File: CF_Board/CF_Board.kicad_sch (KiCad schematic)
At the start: 24 parts, among them J1 Conn_02x04_Odd_Even, SW1 SW_DIP_x08, U1 74FCT16245, U2 74HCT245, U3 22V10, U4 74HCT688, U5 74HCT138, U6 22V10, U7 74LVC1G07, X1 DIN41612_03x32_ABC_VMEbus

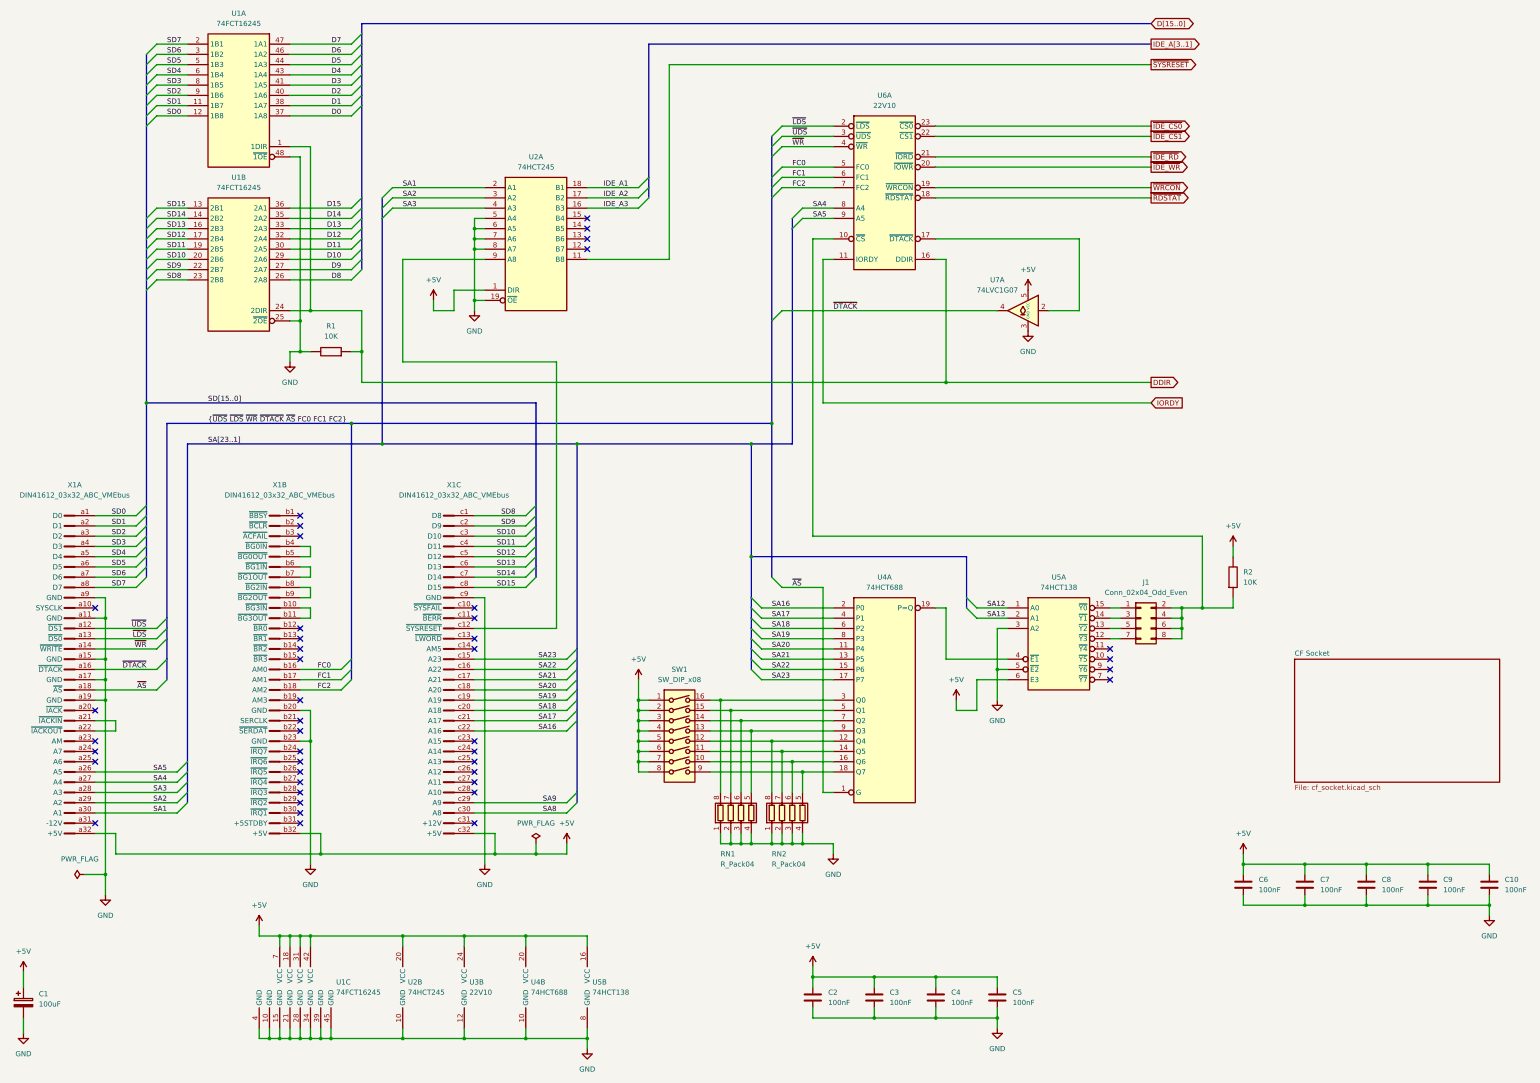
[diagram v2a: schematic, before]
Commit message: Starting PCB layout
* Rearranged signals in the schematic for easier routing
* Rough placement of components on PCB

Still needs a footprint for the CF socket
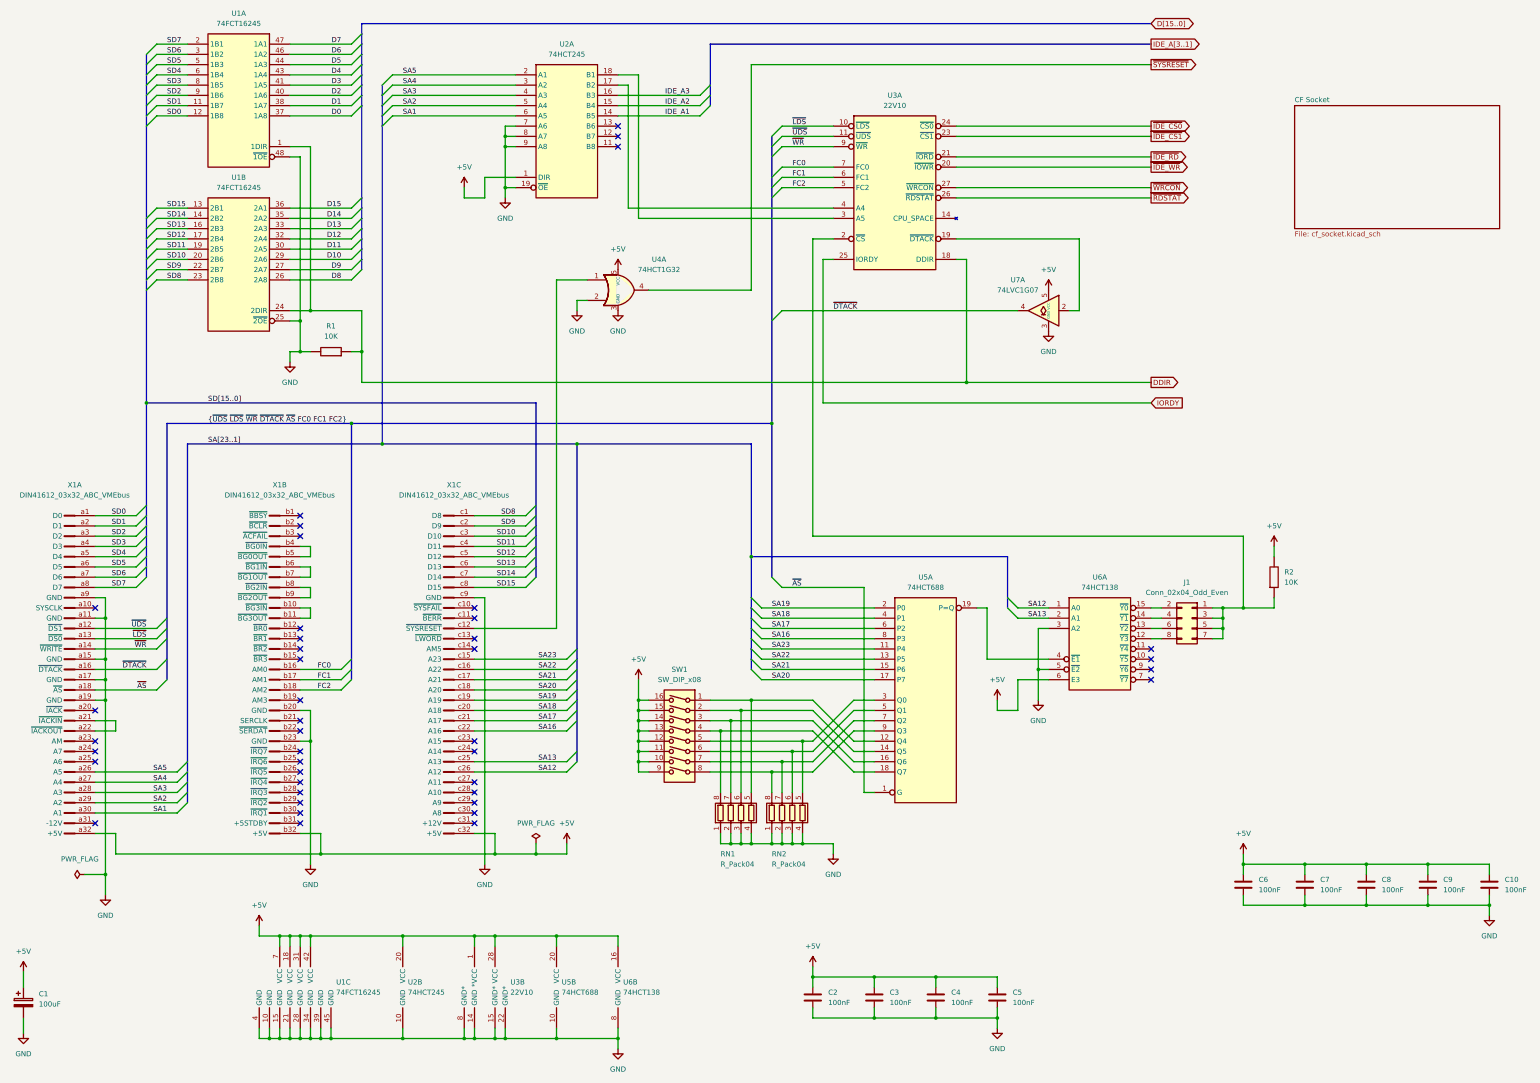
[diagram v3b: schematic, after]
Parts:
- added U4: 74HCT1G32, COMET_footprints:Package_SOT23-5, symbol COMET_symbols:74x1G32
- U3: renamed from U6; footprint Package_DIP:DIP-24_W7.62mm_Socket -> COMET_footprints:Package_PLCC-28_SMD_socket; symbol CF_Board:22V10 -> CF_Board:GAL
- U3: footprint Package_DIP:DIP-24_W7.62mm_Socket -> COMET_footprints:Package_PLCC-28_SMD_socket
- renumbered U4 to U5, U5 to U6
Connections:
- net +5V: now also SW1.10, SW1.11, SW1.12, SW1.13, SW1.14, SW1.15, SW1.16, SW1.9, U3.1 (*VCC), U3.28 (VCC), U4.5 (VCC); no longer SW1.1, SW1.2, SW1.3, SW1.4, SW1.5, SW1.6, SW1.7, SW1.8, U3.24 (VCC)
- net DDIR: now also U3.18 (DDIR); no longer U3.16 (DDIR)
- net FC0: now also U3.7 (FC0); no longer U3.5 (FC0)
- net FC2: now also U3.5 (FC2); no longer U3.7 (FC2)
- net GND: now also U2.9 (A8), U3.14 (GND), U3.15 (GND*), U3.22 (GND*), U3.8 (GND*), U4.2, U4.3 (GND); no longer U2.5 (A4), U2.6 (A5), U3.12 (GND)
- net IDE_A1: now also U2.14 (B5); no longer U2.18 (B1)
- net IDE_A2: now also U2.15 (B4); no longer U2.17 (B2)
- net IORDY: now also U3.25 (IORDY); no longer U3.11 (IORDY)
- net SA1: now also U2.6 (A5); no longer U2.2 (A1)
- net SA12: now also X1.c26 (A12)
- net SA13: now also X1.c25 (A13)
- net SA16: now also U5.8 (P3); no longer U5.2 (P0)
- net SA17: now also U5.6 (P2); no longer U5.4 (P1)
- net SA18: now also U5.4 (P1); no longer U5.6 (P2)
- net SA19: now also U5.2 (P0); no longer U5.8 (P3)
- net SA2: now also U2.5 (A4); no longer U2.3 (A2)
- net SA20: now also U5.17 (P7); no longer U5.11 (P4)
- net SA21: now also U5.15 (P6); no longer U5.13 (P5)
- net SA22: now also U5.13 (P5); no longer U5.15 (P6)
- net SA23: now also U5.11 (P4); no longer U5.17 (P7)
- net SA4: now also U2.3 (A2); no longer U3.8 (A4)
- net SA5: now also U2.2 (A1); no longer U3.9 (A5)
- net ~{IDE_CS0}: now also U3.24 (~{CS0}); no longer U3.23 (~{CS0})
- net ~{IDE_CS1}: now also U3.23 (~{CS1}); no longer U3.22 (~{CS1})
- net ~{LDS}: now also U3.10 (~{LDS}); no longer U3.2 (~{LDS})
- net ~{RDSTAT}: now also U3.26 (~{RDSTAT}); no longer U3.18 (~{RDSTAT})
- net ~{SYSRESET}: now also U4.4; no longer U2.11 (B8)
- net ~{UDS}: now also U3.11 (~{UDS}); no longer U3.3 (~{UDS})
- net ~{WRCON}: now also U3.27 (~{WRCON}); no longer U3.19 (~{WRCON})
- net ~{WR}: now also U3.9 (~{WR}); no longer U3.4 (~{WR})
- net at X1.c12 (~{SYSRESET}): now also U4.1; no longer U2.9 (A8)
- net at J1.1 (Pin_1): now also J1.3 (Pin_3), J1.5 (Pin_5), J1.7 (Pin_7), R2.2, U3.2 (~{CS}); no longer U6.15 (~{Y0})
- net at U6.14 (~{Y1}): now also J1.4 (Pin_4); no longer J1.3 (Pin_3)
- net at U6.13 (~{Y2}): now also J1.6 (Pin_6); no longer J1.5 (Pin_5)
- net at U6.12 (~{Y3}): now also J1.8 (Pin_8); no longer J1.7 (Pin_7)
- net at U7.2: now also U3.19 (~{DTACK}); no longer U3.17 (~{DTACK})
- net SA8: no longer names the net of X1.c30 (A8)
- net SA9: no longer names the net of X1.c29 (A9)
- new net: U2.17 (B2), U3.4 (A4)
- new net: U2.18 (B1), U3.3 (A5)
- new net: J1.2 (Pin_2), U6.15 (~{Y0})
- new net: RN2.5 (R4.2), SW1.5, U5.3 (Q0)
- new net: RN2.6 (R3.2), SW1.6, U5.5 (Q1)
- new net: RN2.7 (R2.2), SW1.7, U5.7 (Q2)
- new net: RN2.8 (R1.2), SW1.8, U5.9 (Q3)
- new net: RN1.5 (R4.2), SW1.1, U5.12 (Q4)
- new net: RN1.6 (R3.2), SW1.2, U5.14 (Q5)
- new net: RN1.7 (R2.2), SW1.3, U5.16 (Q6)
- new net: RN1.8 (R1.2), SW1.4, U5.18 (Q7)
- no-connect marks 43 -> 42
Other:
- moved on the sheet: J1, R2, U2A, U5A, U5B, U6A, U6B, U7A
